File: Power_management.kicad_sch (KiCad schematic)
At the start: 0 parts

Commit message: development stage 1 - testing board for AFE / Fuel gage / high side protection controller - unfinished
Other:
- added sheet Testing Stage 1 MONITORING (monitoring.kicad_sch)
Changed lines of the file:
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@@
 	(text "REGOUT_AFE AT 3.3V?"
 		(exclude_from_sim no)
-		(at 261.62 39.116 0)
+		(at 210.82 63.5 0)
 		(effects
 			(font
@@
 	(text "PMP22805 reference design - includes USB OTG for powering RADA ROCK 5B?"
 		(exclude_from_sim no)
-		(at 129.032 18.034 0)
+		(at 130.81 16.51 0)
 		(effects
 			(font
@@
 				)
 			)
+		)
+	)
+	(sheet
+		(at 20.32 120.65)
+		(size 36.83 34.29)
+		(exclude_from_sim no)
+		(in_bom yes)
+		(on_board yes)
+		(dnp no)
+		(fields_autoplaced yes)
+		(stroke
+			(width 0.1524)
+			(type solid)
+		)
+		(fill
+			(color 0 0 0 0.0000)
+		)
+		(property "Sheetname" "Testing Stage 1 MONITORING"
+			(at 20.32 119.9384 0)
+			(effects
+				(font
+					(size 1.27 1.27)
+				)
+				(justify left bottom)
+			)
+		)
+		(property "Sheetfile" "monitoring.kicad_sch"
+			(at 20.32 155.5246 0)
+			(effects
+				(font
+					(size 1.27 1.27)
+				)
+				(justify left top)
+			)
+		)
+		(instances
+			(project "Power_management"
+				(path "/81e8a54f-a6a6-4f78-985c-1dc7d6751007"
+					(page "9")
+				)
+			)

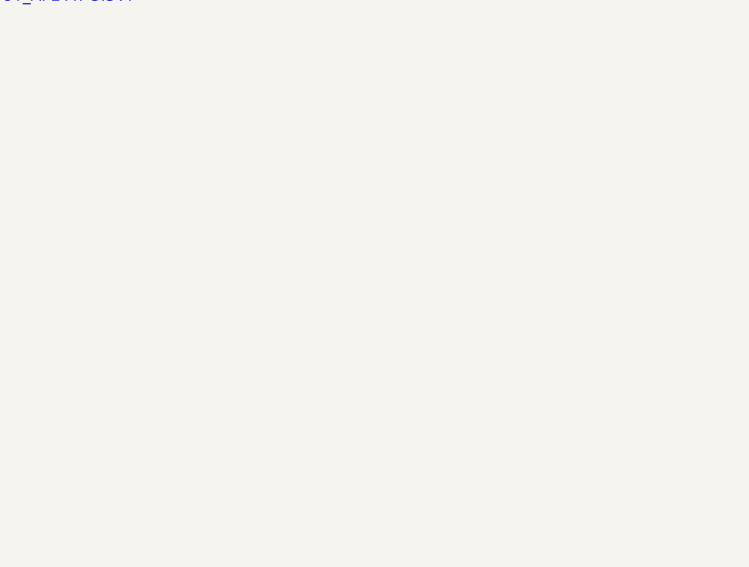
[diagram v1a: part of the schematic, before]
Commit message: refinements - moving battery pack off the PCB
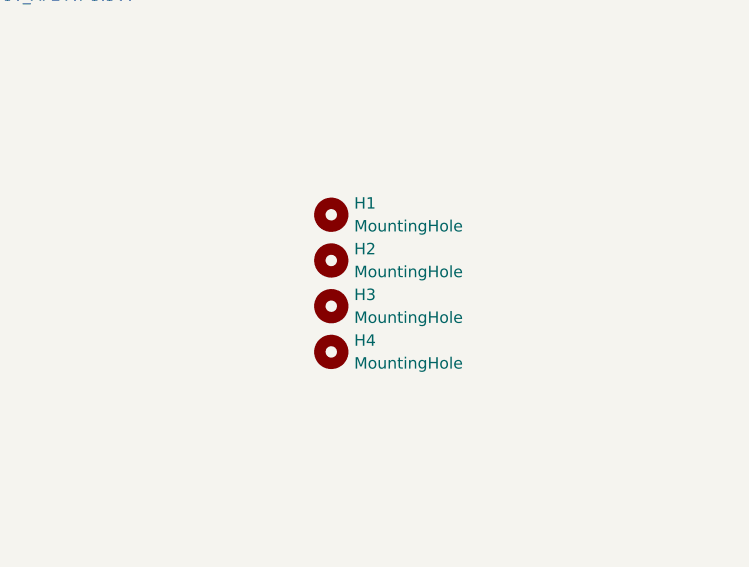
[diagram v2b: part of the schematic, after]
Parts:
- added H1, H2, H3, H4: MountingHole, MountingHole:MountingHole_3.2mm_M3, symbol Mechanical:MountingHole

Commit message: adding charging stages finally
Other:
- removed sheet Testing Stage 1 MONITORING
- sheet Charger IC ports: added 3V3, BATT+, BATT-, PPHV; removed none
- sheet USB Interface ports: added PPHV; removed USB_20V_BUS
- note added: "main current path connections all to be rated to 12A"

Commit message: progress
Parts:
- added J1: Screw_Terminal_01x02, symbol Connector:Screw_Terminal_01x02
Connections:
- new net Cell Monitor/PACK+: J1.1 (Pin_1)
- new net Cell Monitor/PACK-: J1.2 (Pin_2)
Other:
- removed sheet Buck Converter Stage
- removed sheet Power Distribution
